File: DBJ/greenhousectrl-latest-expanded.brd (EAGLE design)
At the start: 160 x 100 mm, 56 parts, among them IC1 ATMEGA168TQFP-08, IC4 L298, J1 5.5x2.1mm Barrel, K1 RELAYPTH4, Q1 MMBT2222A, U2 V_REG_317SMD, X1 CRYSTALS-NOGND-HC49

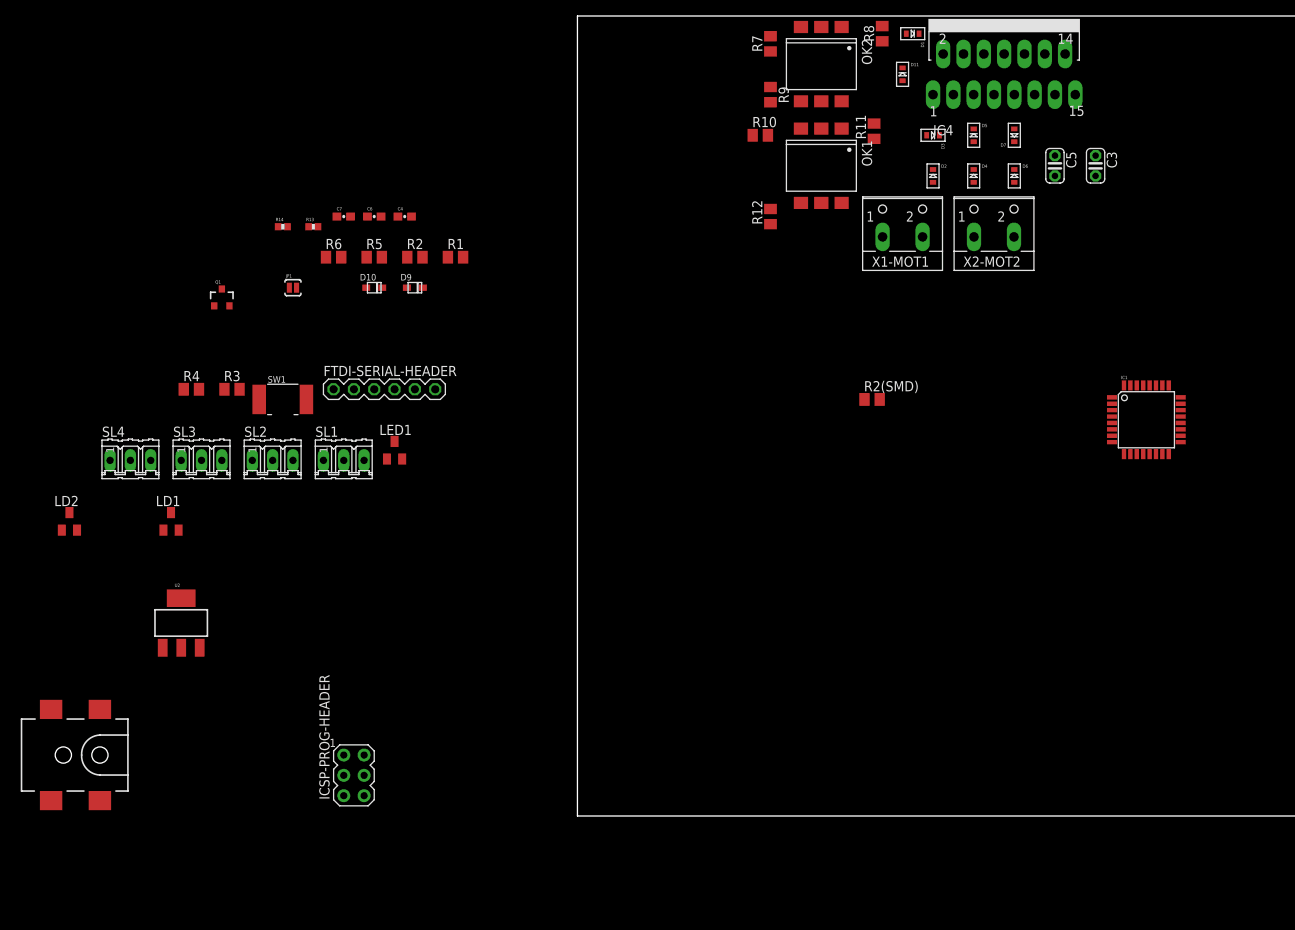
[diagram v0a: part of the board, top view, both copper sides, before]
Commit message: Updated power jack / caps, routed h-bridge and components
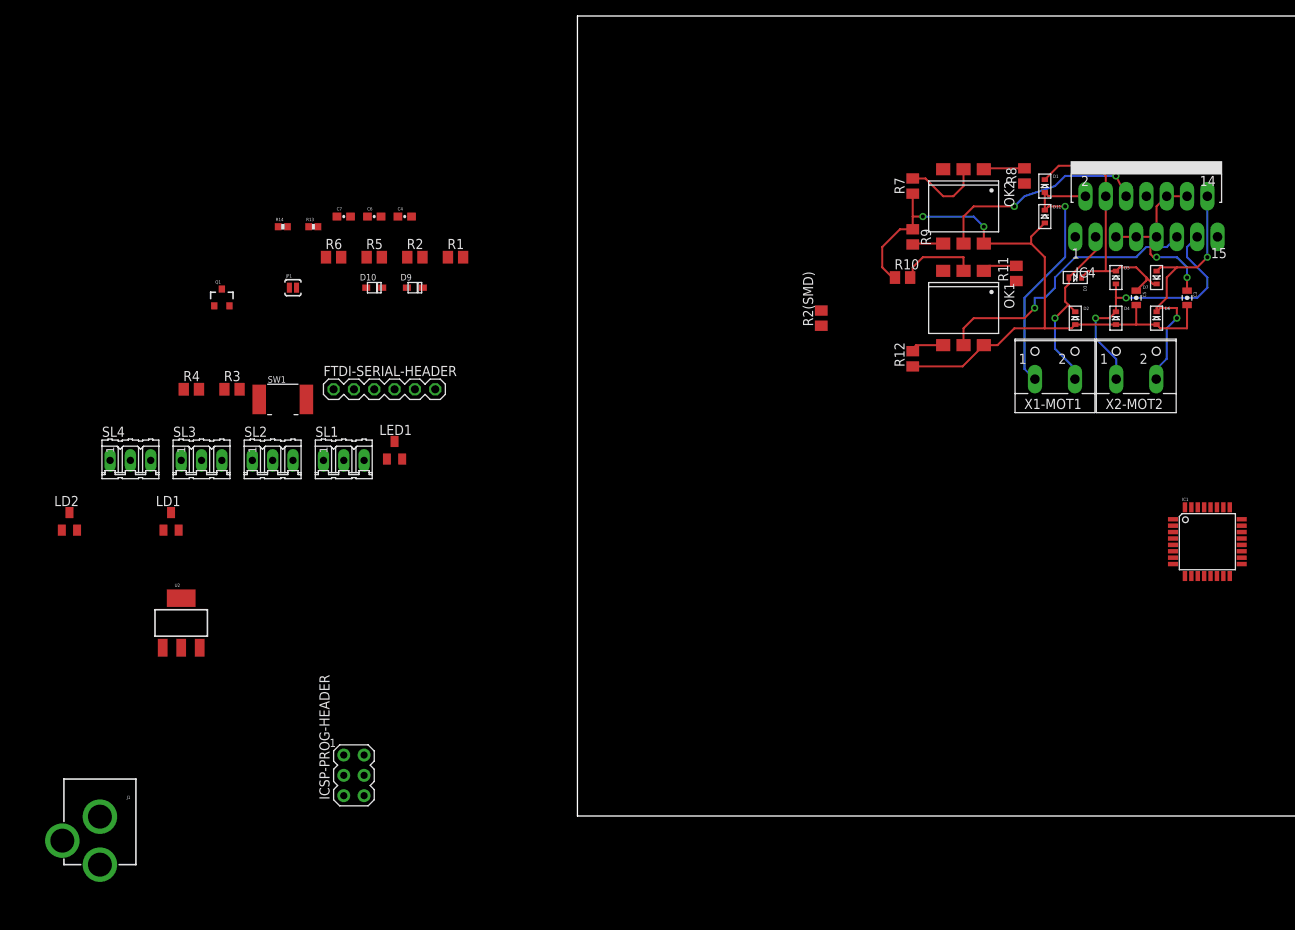
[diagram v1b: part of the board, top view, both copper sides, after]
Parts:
- C3, C5: value (none) -> 1.0uF; device adafruit:C025-024X044 -> SparkFun-Capacitors:0805-CAP
- J1: value 5.5x2.1mm Barrel -> POWER_JACKPTH; device SparkFun-Connectors:POWER_JACK_SMD -> SparkFun-Connectors:POWER_JACK_PTH
- moved X1-MOT1 26.1 mm to (59.7, 55.9)
- moved D1 25.2 mm to (58.4, 78.7), turned to 0 degrees
- moved D4 25.1 mm to (67.3, 62.2)
- moved D5 25.1 mm to (67.3, 67.3)
- moved D6 25.1 mm to (72.4, 62.2)
- moved D7 25.1 mm to (72.4, 67.3)
- moved IC4 25.1 mm to (71.1, 80.0)
- moved R10 25.1 mm to (40.6, 67.3)
- moved R12 25.1 mm to (41.9, 57.1)
- moved R8 25.1 mm to (55.9, 80.0)
- moved D2 25.1 mm to (62.2, 62.2)
- moved OK1 25.1 mm to (48.3, 63.5)
- moved OK2 25.1 mm to (48.3, 76.2)
- moved R7 25.1 mm to (41.9, 78.7)
- moved R9 25.1 mm to (41.9, 72.4)
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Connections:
- net +12V: now also J1.PWR; no longer J1.VIN0
- net GND: now also J1.GNDBREAK; no longer J1.P$4
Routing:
- net GND: track 0.00 -> 87.5 mm, vias 0 -> 2
- net ENB: track 0.00 -> 35.0 mm, vias 0 -> 1
- net OUT3: track 0.00 -> 34.9 mm, vias 0 -> 2
- net OUT1: track 0.00 -> 34.5 mm, vias 0 -> 1
- net OUT4: track 0.00 -> 34.0 mm, vias 0 -> 2
- net +12V: track 0.00 -> 33.7 mm
- net ENA: track 0.00 -> 27.0 mm, vias 0 -> 2
- net +5V: track 0.00 -> 23.9 mm, vias 0 -> 2
- net OUT2: track 0.00 -> 22.5 mm, vias 0 -> 1
- net N$9: track 0.00 -> 9.98 mm
- net N$4: track 0.00 -> 9.90 mm
- net N$1: track 0.00 -> 5.13 mm
- net N$8: track 0.00 -> 4.32 mm
- net N$15: track 0.00 -> 3.99 mm
- net N$5: track 0.00 -> 3.86 mm

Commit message: replaced parts to conform with preferred part list
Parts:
- removed K1: RELAYPTH4, SparkFun-Electromechanical:RELAY-JZC
- removed LD1, LD2: PL006-WCR12, led:SOT23
- removed LED1: PL006-WCR13, led:SOT23
- removed SL1, SL2, SL3, SL4: (no value), con-amp-quick:03P
- removed SW1: (no value), adafruit:BTN_CK_KSS
- added K2: G5LE, relay:G5LE
- added LED3, LED4, LED5: (no value), adafruit:CHIP-LED0805
- added SW2: MOMENTARYBUTTON, ece388:SPST_NO_SMD
- added X2, X3, X4, X5: (no value), ece388:W237-103
- C3, C5: device SparkFun-Capacitors:0805-CAP -> adafruit:C0805
- C4, C6, C7: device SparkFun-Capacitors:0603-CAP -> adafruit:C0805
- moved J1 101.2 mm to (19.1, 71.1)
- moved Q1 90.3 mm to (45.7, 68.6)
- moved JP1 87.7 mm to (52.1, 62.2)
- moved R6 81.2 mm to (49.5, 55.9)
- moved J3 71.9 mm to (88.9, 66.0)
- moved SV1 63.7 mm to (94.0, 44.5)
- moved U2 61.3 mm to (5.08, 52.1)
- moved IC4 52.1 mm to (59.7, 29.2)
- moved C3 52.1 mm to (64.8, 14.0)
- moved D11 52.1 mm to (47.0, 24.1)
- moved OK2 52.1 mm to (36.8, 25.4)
- moved R8 52.1 mm to (44.5, 29.2)
- moved X1-MOT1 52.1 mm to (48.3, 5.08)
- moved C5 52.1 mm to (58.4, 14.0)
- moved D1 52.1 mm to (47.0, 27.9)
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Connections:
- net +5V: now also X2.2, X3.2, X4.2, X5.2; no longer SL1.2, SL2.2, SL3.2, SL4.2
- net COIL: now also K2.2; no longer K1.1
- net COMMON: now also K2.P; no longer K1.4
- net GND: now also LED3.A, LED4.A, SW2.4, X2.1, X3.1, X4.3, X5.3; no longer LD1.3, LD2.3, SL1.1, SL2.1, SL3.1, SL4.1, SW1.P$2
- net N$10: now also LED3.C; no longer LD1.1
- net N$2: now also LED4.C; no longer LD2.1
- net N$3: now also LED5.A; no longer LED1.3
- net NC: now also K2.S; no longer K1.2
- net NO: now also K2.O; no longer K1.3
- net PC0: now also X2.3; no longer SL1.3
- net PC1: now also X3.3; no longer SL2.3
- net PC2: now also X4.1; no longer SL3.3
- net PC3: now also X5.1; no longer SL4.3
- net RST: now also SW2.2; no longer SW1.P$1
- net VCC: now also K2.1, LED5.C; no longer K1.5, LED1.1
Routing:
- net OUT4: track 34.0 -> 35.6 mm
- net OUT3: track 34.9 -> 36.0 mm
